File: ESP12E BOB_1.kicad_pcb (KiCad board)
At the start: 2 copper layers, 39.1 x 54.9 mm, 24 parts, among them M1 ESP-12E, P1 CONN_01X07, P2 CONN_01X13, P3 CONN_01X13, P4 CONN_01X01, P5 CONN_01X01, P6 CONN_01X01, P7 CONN_01X01, Q1 BSS138, Q2 BSS138, SW1 SW_PUSH, U1 1117-3.3

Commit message: ADDED FILES
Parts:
- removed P1: CONN_01X07, Pin_Headers:Pin_Header_Straight_1x07
- removed the P2 at (137.2, 48.3)
- removed REF** (x4): WireConnection_0-8mmDrill, Wire_Connections_Bridges:WireConnection_0-8mmDrill
- added C1: 0.1u, Capacitors_SMD:C_0805_HandSoldering, B.Cu at (152.8, 91.2)
- added C1: 0.1u, Capacitors_SMD:C_0805_HandSoldering, B.Cu at (126.2, 91.2)
- added C1: 0.1u, Capacitors_SMD:C_0805_HandSoldering, B.Cu at (99.7, 91.2)
- added C1: 0.1u, Capacitors_SMD:C_0805_HandSoldering, B.Cu at (73.2, 91.2)
- added C1: 0.1u, Capacitors_SMD:C_0805_HandSoldering, B.Cu at (46.6, 91.2)
- added C1: 0.1u, Capacitors_SMD:C_0805_HandSoldering, B.Cu at (152.8, 47.5)
- added C1: 0.1u, Capacitors_SMD:C_0805_HandSoldering, B.Cu at (126.2, 47.5)
- added C1: 0.1u, Capacitors_SMD:C_0805_HandSoldering, B.Cu at (99.7, 47.5)
- added C1: 0.1u, Capacitors_SMD:C_0805_HandSoldering, B.Cu at (73.2, 47.5)
- added C2: 2u2, Capacitors_SMD:C_0805_HandSoldering, B.Cu at (160.1, 102.1)
- added C2: 2u2, Capacitors_SMD:C_0805_HandSoldering, B.Cu at (133.6, 102.1)
- added C2: 2u2, Capacitors_SMD:C_0805_HandSoldering, B.Cu at (107.1, 102.1)
- added C2: 2u2, Capacitors_SMD:C_0805_HandSoldering, B.Cu at (80.5, 102.1)
- added C2: 2u2, Capacitors_SMD:C_0805_HandSoldering, B.Cu at (54.0, 102.1)
- added C2: 2u2, Capacitors_SMD:C_0805_HandSoldering, B.Cu at (160.1, 58.4)
- added C2: 2u2, Capacitors_SMD:C_0805_HandSoldering, B.Cu at (133.6, 58.4)
- added C2: 2u2, Capacitors_SMD:C_0805_HandSoldering, B.Cu at (107.1, 58.4)
- added C2: 2u2, Capacitors_SMD:C_0805_HandSoldering, B.Cu at (80.5, 58.4)
- added C3: 4u7, Capacitors_Tantalum_SMD:TantalC_SizeA_EIA-3216_Wave, B.Cu at (166.8, 83.3)
- added C3: 4u7, Capacitors_Tantalum_SMD:TantalC_SizeA_EIA-3216_Wave, B.Cu at (140.2, 83.3)
- added C3: 4u7, Capacitors_Tantalum_SMD:TantalC_SizeA_EIA-3216_Wave, B.Cu at (113.7, 83.3)
- added C3: 4u7, Capacitors_Tantalum_SMD:TantalC_SizeA_EIA-3216_Wave, B.Cu at (87.1, 83.3)
- added C3: 4u7, Capacitors_Tantalum_SMD:TantalC_SizeA_EIA-3216_Wave, B.Cu at (60.6, 83.3)
- added C3: 4u7, Capacitors_Tantalum_SMD:TantalC_SizeA_EIA-3216_Wave, B.Cu at (166.8, 39.6)
- added C3: 4u7, Capacitors_Tantalum_SMD:TantalC_SizeA_EIA-3216_Wave, B.Cu at (140.2, 39.6)
- added C3: 4u7, Capacitors_Tantalum_SMD:TantalC_SizeA_EIA-3216_Wave, B.Cu at (113.7, 39.6)
- added C3: 4u7, Capacitors_Tantalum_SMD:TantalC_SizeA_EIA-3216_Wave, B.Cu at (87.1, 39.6)
- added C4: 10u, Capacitors_Tantalum_SMD:TantalC_SizeA_EIA-3216_Wave, B.Cu at (153.8, 83.3)
- added C4: 10u, Capacitors_Tantalum_SMD:TantalC_SizeA_EIA-3216_Wave, B.Cu at (127.3, 83.3)
- added C4: 10u, Capacitors_Tantalum_SMD:TantalC_SizeA_EIA-3216_Wave, B.Cu at (100.7, 83.3)
- added C4: 10u, Capacitors_Tantalum_SMD:TantalC_SizeA_EIA-3216_Wave, B.Cu at (74.2, 83.3)
- added C4: 10u, Capacitors_Tantalum_SMD:TantalC_SizeA_EIA-3216_Wave, B.Cu at (47.6, 83.3)
- added C4: 10u, Capacitors_Tantalum_SMD:TantalC_SizeA_EIA-3216_Wave, B.Cu at (153.8, 39.6)
- added C4: 10u, Capacitors_Tantalum_SMD:TantalC_SizeA_EIA-3216_Wave, B.Cu at (127.3, 39.6)
- added C4: 10u, Capacitors_Tantalum_SMD:TantalC_SizeA_EIA-3216_Wave, B.Cu at (100.7, 39.6)
- added C4: 10u, Capacitors_Tantalum_SMD:TantalC_SizeA_EIA-3216_Wave, B.Cu at (74.2, 39.6)
- added M1: ESP-12E, ESP12E:ESP-12E, F.Cu at (159.9, 95.0)
- added M1: ESP-12E, ESP12E:ESP-12E, F.Cu at (133.3, 95.0)
- added M1: ESP-12E, ESP12E:ESP-12E, F.Cu at (106.8, 95.0)
- added M1: ESP-12E, ESP12E:ESP-12E, F.Cu at (80.3, 95.0)
- added M1: ESP-12E, ESP12E:ESP-12E, F.Cu at (53.7, 95.0)
- added M1: ESP-12E, ESP12E:ESP-12E, F.Cu at (159.9, 51.3)
- added M1: ESP-12E, ESP12E:ESP-12E, F.Cu at (133.3, 51.3)
- added M1: ESP-12E, ESP12E:ESP-12E, F.Cu at (106.8, 51.3)
- added M1: ESP-12E, ESP12E:ESP-12E, F.Cu at (80.3, 51.3)
- added P2: CONN_01X13, Pin_Headers:Pin_Header_Straight_1x13, B.Cu at (171.3, 81.8)
- added P2: CONN_01X13, Pin_Headers:Pin_Header_Straight_1x13, B.Cu at (65.2, 38.1)
- added P2: CONN_01X13, Pin_Headers:Pin_Header_Straight_1x13, B.Cu at (144.8, 81.8)
- added P2: CONN_01X13, Pin_Headers:Pin_Header_Straight_1x13, B.Cu at (118.2, 81.8)
- added P2: CONN_01X13, Pin_Headers:Pin_Header_Straight_1x13, B.Cu at (91.7, 81.8)
- added P2: CONN_01X13, Pin_Headers:Pin_Header_Straight_1x13, B.Cu at (65.2, 81.8)
- added P2: CONN_01X13, Pin_Headers:Pin_Header_Straight_1x13, B.Cu at (171.3, 38.1)
- added P2: CONN_01X13, Pin_Headers:Pin_Header_Straight_1x13, B.Cu at (144.8, 38.1)
- added P2: CONN_01X13, Pin_Headers:Pin_Header_Straight_1x13, B.Cu at (118.2, 38.1)
- added P2: CONN_01X13, Pin_Headers:Pin_Header_Straight_1x13, B.Cu at (91.7, 38.1)
- added P3: CONN_01X13, Pin_Headers:Pin_Header_Straight_1x13, B.Cu at (148.5, 81.8)
- added P3: CONN_01X13, Pin_Headers:Pin_Header_Straight_1x13, B.Cu at (121.9, 81.8)
- added P3: CONN_01X13, Pin_Headers:Pin_Header_Straight_1x13, B.Cu at (95.4, 81.8)
- added P3: CONN_01X13, Pin_Headers:Pin_Header_Straight_1x13, B.Cu at (68.8, 81.8)
- added P3: CONN_01X13, Pin_Headers:Pin_Header_Straight_1x13, B.Cu at (42.3, 81.8)
- added P3: CONN_01X13, Pin_Headers:Pin_Header_Straight_1x13, B.Cu at (148.5, 38.1)
- added P3: CONN_01X13, Pin_Headers:Pin_Header_Straight_1x13, B.Cu at (121.9, 38.1)
- added P3: CONN_01X13, Pin_Headers:Pin_Header_Straight_1x13, B.Cu at (95.4, 38.1)
- added P3: CONN_01X13, Pin_Headers:Pin_Header_Straight_1x13, B.Cu at (68.8, 38.1)
- added P4: CONN_01X01, Connect:1pin, F.Cu at (148.5, 76.7)
- added P4: CONN_01X01, Connect:1pin, F.Cu at (121.9, 76.7)
- added P4: CONN_01X01, Connect:1pin, F.Cu at (95.4, 76.7)
- added P4: CONN_01X01, Connect:1pin, F.Cu at (68.8, 76.7)
- added P4: CONN_01X01, Connect:1pin, F.Cu at (42.3, 76.7)
- added P4: CONN_01X01, Connect:1pin, F.Cu at (148.5, 33.0)
- added P4: CONN_01X01, Connect:1pin, F.Cu at (121.9, 33.0)
- added P4: CONN_01X01, Connect:1pin, F.Cu at (95.4, 33.0)
- added P4: CONN_01X01, Connect:1pin, F.Cu at (68.8, 33.0)
- added P5: CONN_01X01, Connect:1pin, F.Cu at (171.1, 116.1)
- added P5: CONN_01X01, Connect:1pin, F.Cu at (144.5, 116.1)
- added P5: CONN_01X01, Connect:1pin, F.Cu at (118.0, 116.1)
- added P5: CONN_01X01, Connect:1pin, F.Cu at (91.4, 116.1)
- added P5: CONN_01X01, Connect:1pin, F.Cu at (64.9, 116.1)
- added P5: CONN_01X01, Connect:1pin, F.Cu at (171.1, 72.4)
- added P5: CONN_01X01, Connect:1pin, F.Cu at (144.5, 72.4)
- added P5: CONN_01X01, Connect:1pin, F.Cu at (118.0, 72.4)
- added P5: CONN_01X01, Connect:1pin, F.Cu at (91.4, 72.4)
- added P6: CONN_01X01, Connect:1pin, F.Cu at (148.5, 116.1)
- added P6: CONN_01X01, Connect:1pin, F.Cu at (121.9, 116.1)
- added P6: CONN_01X01, Connect:1pin, F.Cu at (95.4, 116.1)
- added P6: CONN_01X01, Connect:1pin, F.Cu at (68.8, 116.1)
- added P6: CONN_01X01, Connect:1pin, F.Cu at (42.3, 116.1)
- added P6: CONN_01X01, Connect:1pin, F.Cu at (148.5, 72.4)
- added P6: CONN_01X01, Connect:1pin, F.Cu at (121.9, 72.4)
- added P6: CONN_01X01, Connect:1pin, F.Cu at (95.4, 72.4)
- added P6: CONN_01X01, Connect:1pin, F.Cu at (68.8, 72.4)
- added P7: CONN_01X01, Connect:1pin, F.Cu at (171.1, 76.7)
- added P7: CONN_01X01, Connect:1pin, F.Cu at (144.5, 76.7)
- added P7: CONN_01X01, Connect:1pin, F.Cu at (118.0, 76.7)
- added P7: CONN_01X01, Connect:1pin, F.Cu at (91.4, 76.7)
- added P7: CONN_01X01, Connect:1pin, F.Cu at (64.9, 76.7)
- added P7: CONN_01X01, Connect:1pin, F.Cu at (171.1, 33.0)
- added P7: CONN_01X01, Connect:1pin, F.Cu at (144.5, 33.0)
- added P7: CONN_01X01, Connect:1pin, F.Cu at (118.0, 33.0)
- added P7: CONN_01X01, Connect:1pin, F.Cu at (91.4, 33.0)
- added P8: CONN_01X07, Pin_Headers:Pin_Header_Straight_1x07, F.Cu at (152.1, 77.0)
- added P8: CONN_01X07, Pin_Headers:Pin_Header_Straight_1x07, F.Cu at (45.9, 33.3)
- added P8: CONN_01X07, Pin_Headers:Pin_Header_Straight_1x07, F.Cu at (125.6, 77.0)
- added P8: CONN_01X07, Pin_Headers:Pin_Header_Straight_1x07, F.Cu at (99.0, 77.0)
- added P8: CONN_01X07, Pin_Headers:Pin_Header_Straight_1x07, F.Cu at (72.5, 77.0)
- added P8: CONN_01X07, Pin_Headers:Pin_Header_Straight_1x07, F.Cu at (45.9, 77.0)
- added P8: CONN_01X07, Pin_Headers:Pin_Header_Straight_1x07, F.Cu at (152.1, 33.3)
- added P8: CONN_01X07, Pin_Headers:Pin_Header_Straight_1x07, F.Cu at (125.6, 33.3)
- added P8: CONN_01X07, Pin_Headers:Pin_Header_Straight_1x07, F.Cu at (99.0, 33.3)
- added P8: CONN_01X07, Pin_Headers:Pin_Header_Straight_1x07, F.Cu at (72.5, 33.3)
- added Q1: BSS138, ESP12E:SOT-23-GDS, B.Cu at (157.4, 90.9)
- added Q1: BSS138, ESP12E:SOT-23-GDS, B.Cu at (130.8, 90.9)
- added Q1: BSS138, ESP12E:SOT-23-GDS, B.Cu at (104.3, 90.9)
- added Q1: BSS138, ESP12E:SOT-23-GDS, B.Cu at (77.7, 90.9)
- added Q1: BSS138, ESP12E:SOT-23-GDS, B.Cu at (51.2, 90.9)
- added Q1: BSS138, ESP12E:SOT-23-GDS, B.Cu at (157.4, 47.2)
- added Q1: BSS138, ESP12E:SOT-23-GDS, B.Cu at (130.8, 47.2)
- added Q1: BSS138, ESP12E:SOT-23-GDS, B.Cu at (104.3, 47.2)
- added Q1: BSS138, ESP12E:SOT-23-GDS, B.Cu at (77.7, 47.2)
- added Q2: BSS138, ESP12E:SOT-23-GDS, B.Cu at (159.9, 98.3)
- added Q2: BSS138, ESP12E:SOT-23-GDS, B.Cu at (133.3, 98.3)
- added Q2: BSS138, ESP12E:SOT-23-GDS, B.Cu at (106.8, 98.3)
- added Q2: BSS138, ESP12E:SOT-23-GDS, B.Cu at (80.3, 98.3)
- added Q2: BSS138, ESP12E:SOT-23-GDS, B.Cu at (53.7, 98.3)
- added Q2: BSS138, ESP12E:SOT-23-GDS, B.Cu at (159.9, 54.6)
- added Q2: BSS138, ESP12E:SOT-23-GDS, B.Cu at (133.3, 54.6)
- added Q2: BSS138, ESP12E:SOT-23-GDS, B.Cu at (106.8, 54.6)
- added Q2: BSS138, ESP12E:SOT-23-GDS, B.Cu at (80.3, 54.6)
- added R1: 470K, Resistors_SMD:R_0603_HandSoldering, B.Cu at (162.4, 90.9)
- added R1: 470K, Resistors_SMD:R_0603_HandSoldering, B.Cu at (135.9, 90.9)
- added R1: 470K, Resistors_SMD:R_0603_HandSoldering, B.Cu at (109.3, 90.9)
- added R1: 470K, Resistors_SMD:R_0603_HandSoldering, B.Cu at (82.8, 90.9)
- added R1: 470K, Resistors_SMD:R_0603_HandSoldering, B.Cu at (56.3, 90.9)
- added R1: 470K, Resistors_SMD:R_0603_HandSoldering, B.Cu at (162.4, 47.2)
- added R1: 470K, Resistors_SMD:R_0603_HandSoldering, B.Cu at (135.9, 47.2)
- added R1: 470K, Resistors_SMD:R_0603_HandSoldering, B.Cu at (109.3, 47.2)
- added R1: 470K, Resistors_SMD:R_0603_HandSoldering, B.Cu at (82.8, 47.2)
- added R2: 100K, Resistors_SMD:R_0603_HandSoldering, B.Cu at (163.4, 95.0)
- added R2: 100K, Resistors_SMD:R_0603_HandSoldering, B.Cu at (136.9, 95.0)
- added R2: 100K, Resistors_SMD:R_0603_HandSoldering, B.Cu at (110.4, 95.0)
- added R2: 100K, Resistors_SMD:R_0603_HandSoldering, B.Cu at (83.8, 95.0)
- added R2: 100K, Resistors_SMD:R_0603_HandSoldering, B.Cu at (57.3, 95.0)
- added R2: 100K, Resistors_SMD:R_0603_HandSoldering, B.Cu at (163.4, 51.3)
- added R2: 100K, Resistors_SMD:R_0603_HandSoldering, B.Cu at (136.9, 51.3)
- added R2: 100K, Resistors_SMD:R_0603_HandSoldering, B.Cu at (110.4, 51.3)
- added R2: 100K, Resistors_SMD:R_0603_HandSoldering, B.Cu at (83.8, 51.3)
- added R3: 10K, Resistors_SMD:R_0603_HandSoldering, B.Cu at (164.5, 102.1)
- added R3: 10K, Resistors_SMD:R_0603_HandSoldering, B.Cu at (137.9, 102.1)
- added R3: 10K, Resistors_SMD:R_0603_HandSoldering, B.Cu at (111.4, 102.1)
- added R3: 10K, Resistors_SMD:R_0603_HandSoldering, B.Cu at (84.8, 102.1)
- added R3: 10K, Resistors_SMD:R_0603_HandSoldering, B.Cu at (58.3, 102.1)
- added R3: 10K, Resistors_SMD:R_0603_HandSoldering, B.Cu at (164.5, 58.4)
- added R3: 10K, Resistors_SMD:R_0603_HandSoldering, B.Cu at (137.9, 58.4)
- added R3: 10K, Resistors_SMD:R_0603_HandSoldering, B.Cu at (111.4, 58.4)
- added R3: 10K, Resistors_SMD:R_0603_HandSoldering, B.Cu at (84.8, 58.4)
- added R4: 47K, Resistors_SMD:R_0603_HandSoldering, B.Cu at (166.0, 91.9)
- added R4: 47K, Resistors_SMD:R_0603_HandSoldering, B.Cu at (139.4, 91.9)
- added R4: 47K, Resistors_SMD:R_0603_HandSoldering, B.Cu at (112.9, 91.9)
- added R4: 47K, Resistors_SMD:R_0603_HandSoldering, B.Cu at (86.4, 91.9)
- added R4: 47K, Resistors_SMD:R_0603_HandSoldering, B.Cu at (59.8, 91.9)
- added R4: 47K, Resistors_SMD:R_0603_HandSoldering, B.Cu at (166.0, 48.3)
- added R4: 47K, Resistors_SMD:R_0603_HandSoldering, B.Cu at (139.4, 48.3)
- added R4: 47K, Resistors_SMD:R_0603_HandSoldering, B.Cu at (112.9, 48.3)
- added R4: 47K, Resistors_SMD:R_0603_HandSoldering, B.Cu at (86.4, 48.3)
- added SW1: SW_PUSH, ESP12E:SW_PUSH_SMALL_2pin_xl, F.Cu at (160.1, 110.7)
- added SW1: SW_PUSH, ESP12E:SW_PUSH_SMALL_2pin_xl, F.Cu at (133.6, 110.7)
- added SW1: SW_PUSH, ESP12E:SW_PUSH_SMALL_2pin_xl, F.Cu at (107.1, 110.7)
- added SW1: SW_PUSH, ESP12E:SW_PUSH_SMALL_2pin_xl, F.Cu at (80.5, 110.7)
- added SW1: SW_PUSH, ESP12E:SW_PUSH_SMALL_2pin_xl, F.Cu at (54.0, 110.7)
- added SW1: SW_PUSH, ESP12E:SW_PUSH_SMALL_2pin_xl, F.Cu at (160.1, 67.1)
- added SW1: SW_PUSH, ESP12E:SW_PUSH_SMALL_2pin_xl, F.Cu at (133.6, 67.1)
- added SW1: SW_PUSH, ESP12E:SW_PUSH_SMALL_2pin_xl, F.Cu at (107.1, 67.1)
- added SW1: SW_PUSH, ESP12E:SW_PUSH_SMALL_2pin_xl, F.Cu at (80.5, 67.1)
- added U1: 1117-3.3, SMD_Packages:SOT-223, B.Cu at (160.4, 82.5)
- added U1: 1117-3.3, SMD_Packages:SOT-223, B.Cu at (133.9, 82.5)
- added U1: 1117-3.3, SMD_Packages:SOT-223, B.Cu at (107.3, 82.5)
- added U1: 1117-3.3, SMD_Packages:SOT-223, B.Cu at (80.8, 82.5)
- added U1: 1117-3.3, SMD_Packages:SOT-223, B.Cu at (54.2, 82.5)
- added U1: 1117-3.3, SMD_Packages:SOT-223, B.Cu at (160.4, 38.9)
- added U1: 1117-3.3, SMD_Packages:SOT-223, B.Cu at (133.9, 38.9)
- added U1: 1117-3.3, SMD_Packages:SOT-223, B.Cu at (107.3, 38.9)
- added U1: 1117-3.3, SMD_Packages:SOT-223, B.Cu at (80.8, 38.9)
- P3: moved to B.Cu
- moved M1 72.7 mm to (53.7, 51.3)
- moved Q2 72.7 mm to (53.7, 54.6)
- moved R1 72.7 mm to (56.3, 47.2)
- moved C4 72.7 mm to (47.6, 39.6)
- moved P3 72.7 mm to (42.3, 38.1), turned to 180 degrees
- moved P4 72.7 mm to (42.3, 33.0)
- moved P5 72.7 mm to (64.9, 72.4)
- moved P6 72.7 mm to (42.3, 72.4)
- moved P7 72.7 mm to (64.9, 33.0)
- moved Q1 72.7 mm to (51.2, 47.2)
- moved R2 72.7 mm to (57.3, 51.3)
- moved U1 72.7 mm to (54.2, 38.9)
- moved C1 72.7 mm to (46.6, 47.5)
- moved C2 72.7 mm to (54.0, 58.4)
- moved C3 72.7 mm to (60.6, 39.6)
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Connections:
- M1 pad 21: /TX -> /RX
- M1 pad 22: /RX -> /TX
- M1 pad 8: Net-(M1-Pad8) -> +3V3
- P3 pad 10: Net-(M1-Pad8) -> +3V3
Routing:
- net GND: track 115.8 -> 1203.7 mm, vias 2 -> 20
- net +3V3: track 27.3 -> 705.4 mm, vias 0 -> 20
- net /DTR: track 54.0 -> 676.8 mm, vias 0 -> 20
- net Net-(M1-Pad11): track 19.5 -> 282.1 mm
- net /TX: track 23.9 -> 246.9 mm
- net /RX: track 25.3 -> 246.9 mm, vias 2 -> 0
- net +5V: track 26.6 -> 246.6 mm
- net Net-(M1-Pad10): track 12.5 -> 214.1 mm
- net Net-(M1-Pad3): track 18.0 -> 196.1 mm, vias 1 -> 10
- net /GPIO10: track 18.5 -> 188.4 mm
- net /SCK: track 8.13 -> 164.4 mm
- net Net-(Q1-PadD): track 10.2 -> 144.8 mm
- net Net-(M1-Pad16): track 11.2 -> 127.8 mm
- net /MOSI: track 12.4 -> 119.9 mm
- net /GPIO0: track 11.5 -> 115.0 mm, vias 1 -> 10
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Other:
- board size 39.1 x 54.9 mm -> 132.6 x 87.1 mm
- net class Default: clearance 0.5 -> 0.1778
- rule trace_clearance: 0.5 -> 0.1778
- board text added: "0"
- board text added: "10"
- board text added: "12"
- board text added: "13"
- board text added: "14"
- board text added: "15"
- board text added: "16"
- board text added: "2"
- board text added: "3.3"
- board text added: "4"
- board text added: "5"
- board text added: "5V"
- board text added: "9"
- board text added: "ADC"
- board text added: "CSO"
- board text added: "C_P"
- board text added: "DTR"
- board text added: "ESP12E WIFI"
- board text added: "ExploreEmbedded.com"
- board text added: "G"
- board text added: "MISO"
- board text added: "MOSI"
- board text added: "RST"
- board text added: "RX"
- board text added: "SCK"
- board text added: "TX"
- board text removed: "1. module 3.3V no connected. 2. UART connections 3. Keep board mounting holes 2mm. 4. Labels should be reflect on the baord."

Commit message: ADDED NEW FILES
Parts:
- removed the C1 at (152.8, 91.2)
- removed the C1 at (126.2, 91.2)
- removed the C1 at (99.7, 91.2)
- removed the C1 at (73.2, 91.2)
- removed the C1 at (46.6, 91.2)
- removed the C1 at (152.8, 47.5)
- removed the C1 at (126.2, 47.5)
- removed the C1 at (99.7, 47.5)
- removed the C1 at (73.2, 47.5)
- removed the C2 at (160.1, 102.1)
- removed the C2 at (133.6, 102.1)
- removed the C2 at (107.1, 102.1)
- removed the C2 at (80.5, 102.1)
- removed the C2 at (54.0, 102.1)
- removed the C2 at (160.1, 58.4)
- removed the C2 at (133.6, 58.4)
- removed the C2 at (107.1, 58.4)
- removed the C2 at (80.5, 58.4)
- removed the C3 at (166.8, 83.3)
- removed the C3 at (60.6, 39.6)
- removed the C3 at (140.2, 83.3)
- removed the C3 at (113.7, 83.3)
- removed the C3 at (87.1, 83.3)
- removed the C3 at (60.6, 83.3)
- removed the C3 at (166.8, 39.6)
- removed the C3 at (140.2, 39.6)
- removed the C3 at (113.7, 39.6)
- removed the C3 at (87.1, 39.6)
- removed the C4 at (153.8, 83.3)
- removed the C4 at (127.3, 83.3)
- removed the C4 at (100.7, 83.3)
- removed the C4 at (74.2, 83.3)
- removed the C4 at (47.6, 83.3)
- removed the C4 at (153.8, 39.6)
- removed the C4 at (127.3, 39.6)
- removed the C4 at (100.7, 39.6)
- removed the C4 at (74.2, 39.6)
- removed the M1 at (159.9, 95.0)
- removed the M1 at (133.3, 95.0)
- removed the M1 at (106.8, 95.0)
- removed the M1 at (80.3, 95.0)
- removed the M1 at (53.7, 95.0)
- removed the M1 at (159.9, 51.3)
- removed the M1 at (133.3, 51.3)
- removed the M1 at (106.8, 51.3)
- removed the M1 at (80.3, 51.3)
- removed the P2 at (171.3, 81.8)
- removed the P2 at (65.2, 38.1)
- removed the P2 at (144.8, 81.8)
- removed the P2 at (118.2, 81.8)
- removed the P2 at (91.7, 81.8)
- removed the P2 at (65.2, 81.8)
- removed the P2 at (171.3, 38.1)
- removed the P2 at (144.8, 38.1)
- removed the P2 at (118.2, 38.1)
- removed the P2 at (91.7, 38.1)
- removed the P3 at (148.5, 81.8)
- removed the P3 at (121.9, 81.8)
- removed the P3 at (95.4, 81.8)
- removed the P3 at (68.8, 81.8)
- removed the P3 at (42.3, 81.8)
- removed the P3 at (148.5, 38.1)
- removed the P3 at (121.9, 38.1)
- removed the P3 at (95.4, 38.1)
- removed the P3 at (68.8, 38.1)
- removed the P4 at (148.5, 76.7)
- removed the P4 at (121.9, 76.7)
- removed the P4 at (95.4, 76.7)
- removed the P4 at (68.8, 76.7)
- removed the P4 at (42.3, 76.7)
- removed the P4 at (148.5, 33.0)
- removed the P4 at (121.9, 33.0)
- removed the P4 at (95.4, 33.0)
- removed the P4 at (68.8, 33.0)
- removed the P5 at (171.1, 116.1)
- removed the P5 at (144.5, 116.1)
- removed the P5 at (118.0, 116.1)
- removed the P5 at (91.4, 116.1)
- removed the P5 at (64.9, 116.1)
- removed the P5 at (171.1, 72.4)
- removed the P5 at (144.5, 72.4)
- removed the P5 at (118.0, 72.4)
- removed the P5 at (91.4, 72.4)
- removed the P6 at (148.5, 116.1)
- removed the P6 at (121.9, 116.1)
- removed the P6 at (95.4, 116.1)
- removed the P6 at (68.8, 116.1)
- removed the P6 at (42.3, 116.1)
- removed the P6 at (148.5, 72.4)
- removed the P6 at (121.9, 72.4)
- removed the P6 at (95.4, 72.4)
- removed the P6 at (68.8, 72.4)
- removed the P7 at (171.1, 76.7)
- removed the P7 at (144.5, 76.7)
- removed the P7 at (118.0, 76.7)
- removed the P7 at (91.4, 76.7)
- removed the P7 at (64.9, 76.7)
- removed the P7 at (171.1, 33.0)
- removed the P7 at (144.5, 33.0)
- removed the P7 at (118.0, 33.0)
- removed the P7 at (91.4, 33.0)
- removed P8 (x10): CONN_01X07, Pin_Headers:Pin_Header_Straight_1x07
- removed the Q1 at (157.4, 90.9)
- removed the Q1 at (130.8, 90.9)
- removed the Q1 at (104.3, 90.9)
- removed the Q1 at (77.7, 90.9)
- removed the Q1 at (51.2, 90.9)
- removed the Q1 at (157.4, 47.2)
- removed the Q1 at (130.8, 47.2)
- removed the Q1 at (104.3, 47.2)
- removed the Q1 at (77.7, 47.2)
- removed the Q2 at (159.9, 98.3)
- removed the Q2 at (133.3, 98.3)
- removed the Q2 at (106.8, 98.3)
- removed the Q2 at (80.3, 98.3)
- removed the Q2 at (53.7, 98.3)
- removed the Q2 at (159.9, 54.6)
- removed the Q2 at (133.3, 54.6)
- removed the Q2 at (106.8, 54.6)
- removed the Q2 at (80.3, 54.6)
- removed the R1 at (162.4, 90.9)
- removed the R1 at (135.9, 90.9)
- removed the R1 at (109.3, 90.9)
- removed the R1 at (82.8, 90.9)
- removed the R1 at (56.3, 90.9)
- removed the R1 at (162.4, 47.2)
- removed the R1 at (135.9, 47.2)
- removed the R1 at (109.3, 47.2)
- removed the R1 at (82.8, 47.2)
- removed the R2 at (163.4, 95.0)
- removed the R2 at (136.9, 95.0)
- removed the R2 at (110.4, 95.0)
- removed the R2 at (83.8, 95.0)
- removed the R2 at (57.3, 95.0)
- removed the R2 at (163.4, 51.3)
- removed the R2 at (136.9, 51.3)
- removed the R2 at (110.4, 51.3)
- removed the R2 at (83.8, 51.3)
- removed the R3 at (164.5, 102.1)
- removed the R3 at (137.9, 102.1)
- removed the R3 at (111.4, 102.1)
- removed the R3 at (84.8, 102.1)
- removed the R3 at (58.3, 102.1)
- removed the R3 at (164.5, 58.4)
- removed the R3 at (137.9, 58.4)
- removed the R3 at (111.4, 58.4)
- removed the R3 at (84.8, 58.4)
- removed the R4 at (166.0, 91.9)
- removed the R4 at (139.4, 91.9)
- removed the R4 at (112.9, 91.9)
- removed the R4 at (86.4, 91.9)
- removed the R4 at (59.8, 91.9)
- removed the R4 at (166.0, 48.3)
- removed the R4 at (139.4, 48.3)
- removed the R4 at (112.9, 48.3)
- removed the R4 at (86.4, 48.3)
- removed the SW1 at (160.1, 110.7)
- removed the SW1 at (133.6, 110.7)
- removed the SW1 at (107.1, 110.7)
- removed the SW1 at (80.5, 110.7)
- removed the SW1 at (54.0, 110.7)
- removed the SW1 at (160.1, 67.1)
- removed the SW1 at (133.6, 67.1)
- removed the SW1 at (107.1, 67.1)
- removed the SW1 at (80.5, 67.1)
- removed the U1 at (160.4, 82.5)
- removed the U1 at (133.9, 82.5)
- removed the U1 at (107.3, 82.5)
- removed the U1 at (80.8, 82.5)
- removed the U1 at (54.2, 82.5)
- removed the U1 at (160.4, 38.9)
- removed the U1 at (133.9, 38.9)
- removed the U1 at (107.3, 38.9)
- removed the U1 at (80.8, 38.9)
- added C3: 4u7, Capacitors_Tantalum_SMD:TantalC_SizeA_EIA-3216_Wave, B.Cu at (132.6, 49.8)
- added LOGO: , logo:LOGO (2), B.Cu at (130.8, 69.6)
- added P1: CONN_01X07, Pin_Headers:Pin_Header_Straight_1x07, F.Cu at (117.9, 42.9)
- added P2: CONN_01X13, Pin_Headers:Pin_Header_Straight_1x13, F.Cu at (137.2, 48.3)
- P3: moved to F.Cu
- moved SW1 72.9 mm to (126.0, 78.2)
- moved M1 72.7 mm to (125.7, 61.5)
- moved Q2 72.7 mm to (125.7, 64.8)
- moved R1 72.7 mm to (128.3, 57.4)
- moved C4 72.7 mm to (119.6, 49.8)
- moved P3 72.7 mm to (114.3, 48.3), turned to 0 degrees
- moved P4 72.7 mm to (114.3, 43.2)
- moved P5 72.7 mm to (136.9, 82.5)
- moved P6 72.7 mm to (114.3, 82.5)
- moved P7 72.7 mm to (136.9, 43.2)
- moved Q1 72.7 mm to (123.2, 57.4)
- moved R2 72.7 mm to (129.3, 61.5)
- moved U1 72.7 mm to (126.2, 49.0)
- moved C1 72.7 mm to (118.6, 57.7)
- moved C2 72.7 mm to (126.0, 68.6)
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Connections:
- net /DTR renamed /RESET
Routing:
- net GND: track 1203.7 -> 123.5 mm, vias 20 -> 2
- net +3V3: track 705.4 -> 70.6 mm, vias 20 -> 2
- net /RESET: track 676.8 -> 73.5 mm, vias 20 -> 2
- net Net-(M1-Pad11): track 282.1 -> 20.0 mm
- net +5V: track 246.6 -> 24.8 mm
- net /RX: track 246.9 -> 28.2 mm
- net /TX: track 246.9 -> 34.9 mm
- net Net-(M1-Pad10): track 214.1 -> 21.4 mm
- net Net-(M1-Pad3): track 196.1 -> 18.3 mm, vias 10 -> 1
- net /GPIO10: track 188.4 -> 19.7 mm
- net /SCK: track 164.4 -> 11.1 mm
- net Net-(Q1-PadD): track 144.8 -> 10.2 mm
- net Net-(M1-Pad16): track 127.8 -> 15.6 mm
- net /MOSI: track 119.9 -> 11.9 mm
- net /GPIO0: track 115.0 -> 15.4 mm, vias 10 -> 1
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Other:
- board size 132.6 x 87.1 mm -> 26.4 x 43.4 mm
- net class Default: clearance 0.1778 -> 0.5
- rule trace_clearance: 0.1778 -> 0.5
- board text added: "NC"

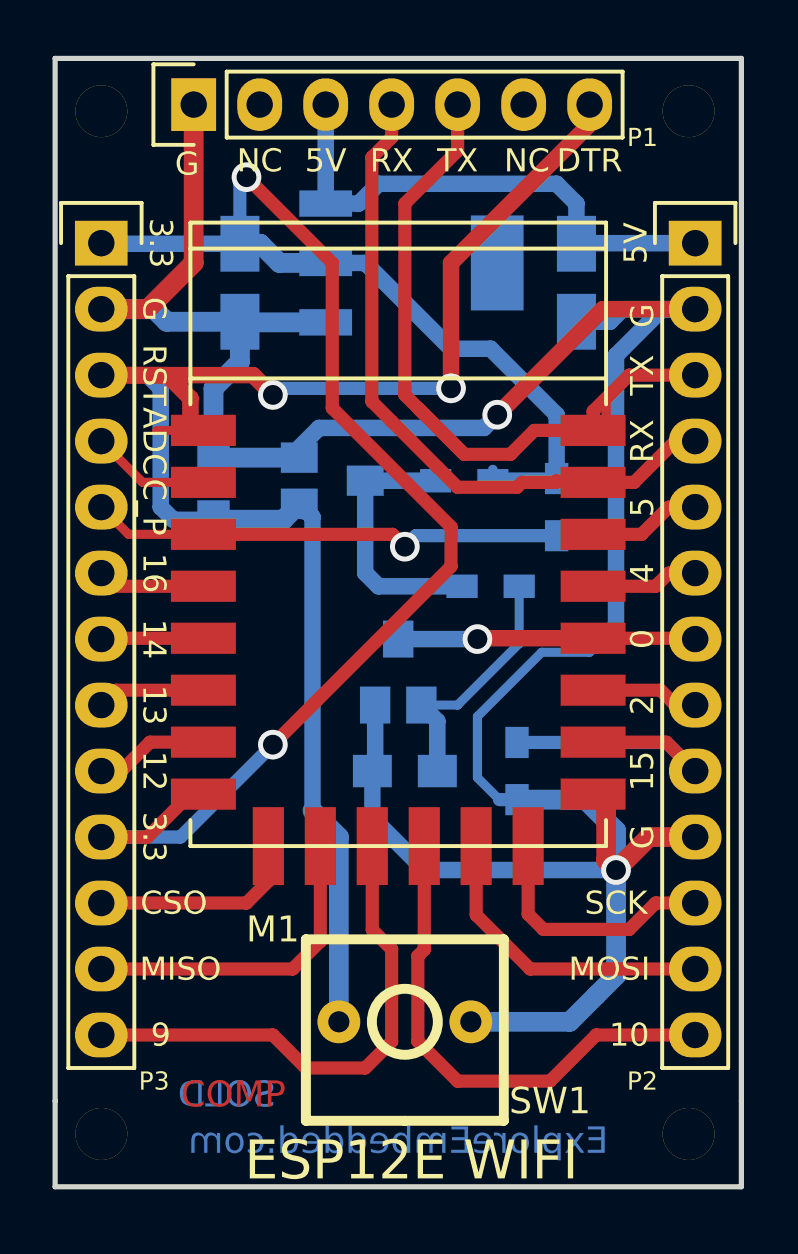
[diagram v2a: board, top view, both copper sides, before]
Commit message: Changed legend and Connector
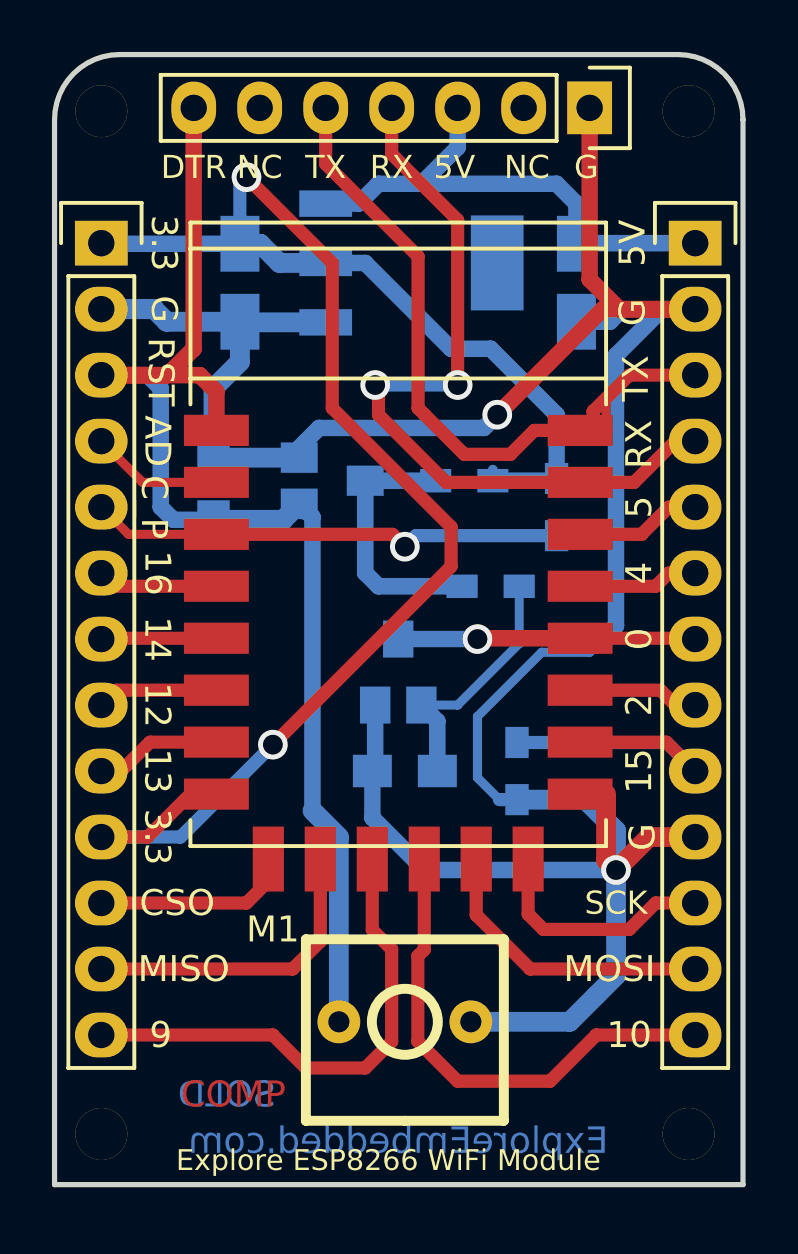
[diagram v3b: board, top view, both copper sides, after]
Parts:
- moved P1 15.2 mm to (133.1, 43.1), turned to 270 degrees
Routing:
- net /RESET: track 73.5 -> 57.2 mm, vias 2 -> 0
- net /RX: track 28.2 -> 31.9 mm, vias 0 -> 2
- net /TX: track 34.9 -> 31.7 mm
- net GND: track 123.5 -> 124.2 mm
- added copper zone on F.Cu, net +3V3
- added copper zone on B.Cu, net GND
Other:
- board size 26.4 x 43.4 mm -> 26.5 x 43.5 mm
- net class Default: clearance 0.5 -> 0.3
- rule trace_clearance: 0.5 -> 0.3
- board text added: "AD"
- board text added: "Explore ESP8266 WiFi Module"
- board text removed: "ADC"
- board text removed: "ESP12E WIFI"
